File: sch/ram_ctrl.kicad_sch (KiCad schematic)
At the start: 12 parts

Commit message: RAM ctrl updates
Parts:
- gave numbers to parts that had none: 1
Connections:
- net z4: now reaches D48.1 (~{R}), D49.10 (O5)
- net at D48.6 (~{Q}): now also D18.2
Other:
- note added: "FIXME: z5 or z6 ?!"
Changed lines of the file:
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@@
+    (stroke (width 0) (type default) (color 0 0 0 0))
+  )
+  (wire (pts (xy 225.425 90.17) (xy 227.965 90.17))
     (stroke (width 0) (type default) (color 0 0 0 0))
   )
@@
     (stroke (width 0) (type default) (color 0 0 0 0))
   )
+  (text "FIXME: z5 or z6 ?!" (at 53.975 147.955 0)
+    (effects (font (size 1.27 1.27)) (justify left bottom))
+  )
   (label "VIDEO-CPU" (at 51.435 137.16 0)
     (effects (font (size 1.27 1.27)) (justify left bottom))
@@
   )
   (label "t2" (at 150.495 62.23 0)
+    (effects (font (size 1.27 1.27)) (justify left bottom))
+  )
+  (label "z4" (at 199.39 69.85 0)
     (effects (font (size 1.27 1.27)) (justify left bottom))
   )
@@
     (pin "1")
   )
-  (symbol (lib_id "74xx:74LS08") (at 162.56 138.43 0) (unit 3) (convert 2)
+  (symbol (lib_id "74xx:74LS08") (at 162.56 138.43 0) (unit 3)
     (in_bom yes) (on_board yes)
     (property "Reference" "D47" (id 0) (at 161.925 143.51 0))
@@
   (symbol (lib_id "74xx:74LS74") (at 247.015 66.04 0) (unit 2)
     (in_bom yes) (on_board yes) (fields_autoplaced)
-    (property "Reference" "D?" (id 0) (at 249.0344 55.88 0)
-      (effects (font (size 1.27 1.27)) (justify left))
-    )
+    (property "Reference" "D48" (id 0) (at 249.0344 55.88 0)
+      (effects (font (size 1.27 1.27)) (justify left))
+    )

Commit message: RAM controller - rework
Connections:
- net VIDEO_CPU: no longer D42.13 (~{R}), D42.4 (~{S})
- new net VIDEO-CPU: D42.13 (~{R}), D42.4 (~{S})
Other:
- moved on the sheet: D18A, D18B, D33D, D33F, D42A, D42B, D46A, D46B, D47A, D47C, D48A, D48B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

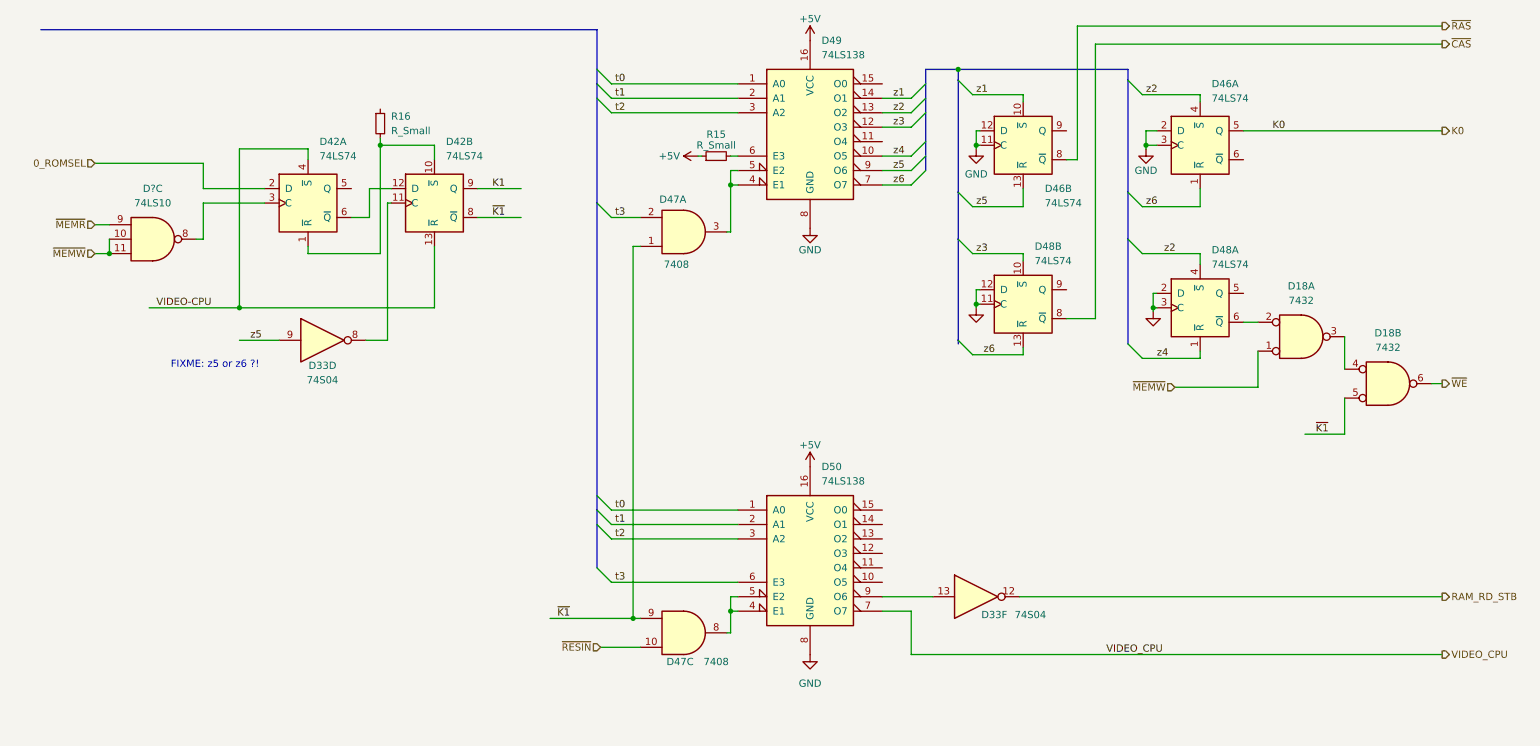
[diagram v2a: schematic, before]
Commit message: RAM ctrl schematic cleanup completed
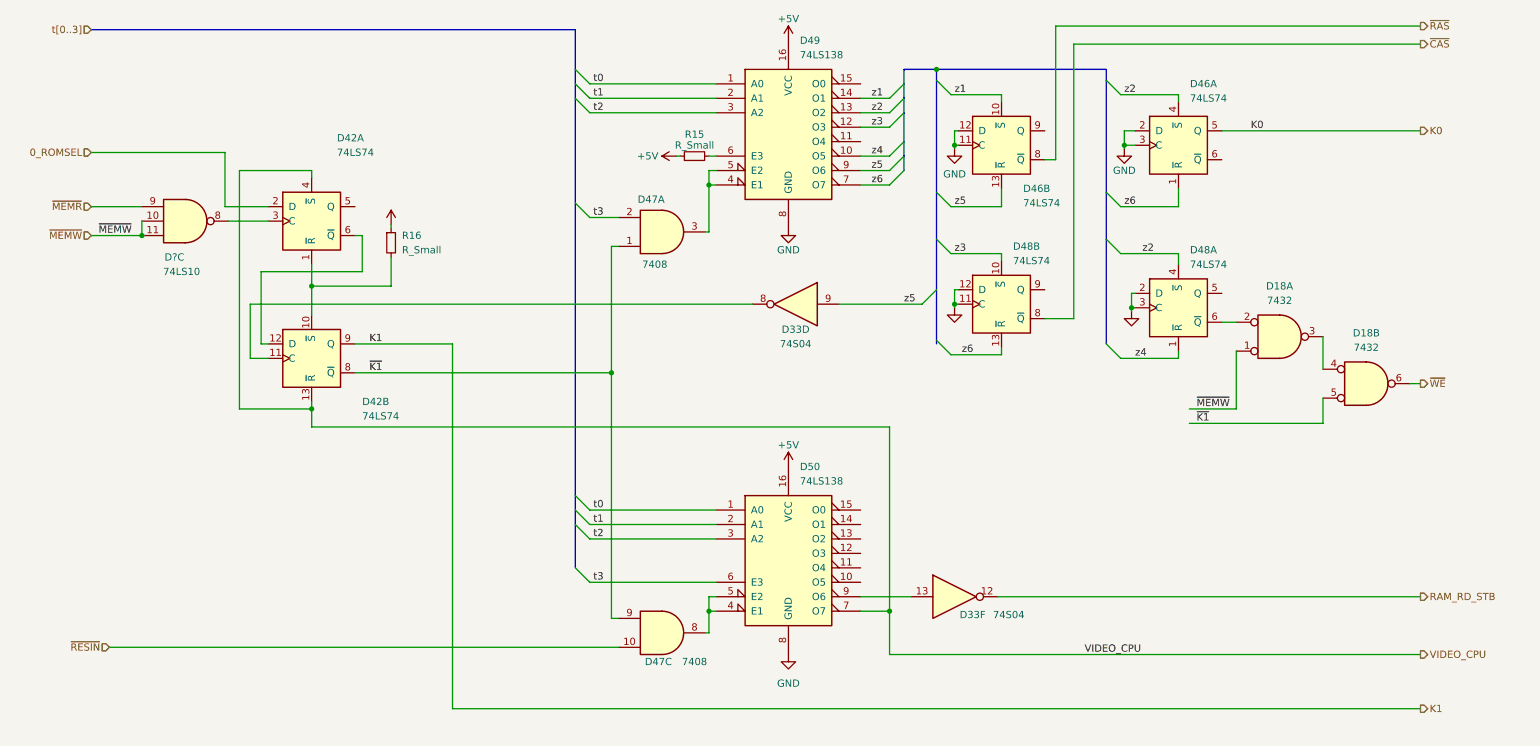
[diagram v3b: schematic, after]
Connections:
- net VIDEO-CPU is gone; now on net VIDEO_CPU: D42.13 (~{R}), D42.4 (~{S})
- net +5V: now also R16.1
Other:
- note removed: "FIXME: z5 or z6 ?!"
- moved on the sheet: D18A, D18B, D33D, D33F, D42A, D42B, D46A, D46B, D47A, D47C, D48A, D48B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

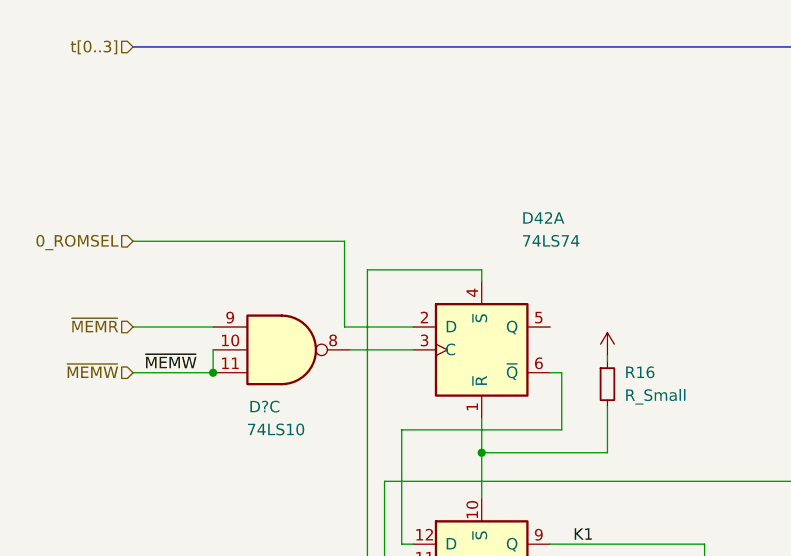
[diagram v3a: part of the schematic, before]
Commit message: Sch: timing counters block completed
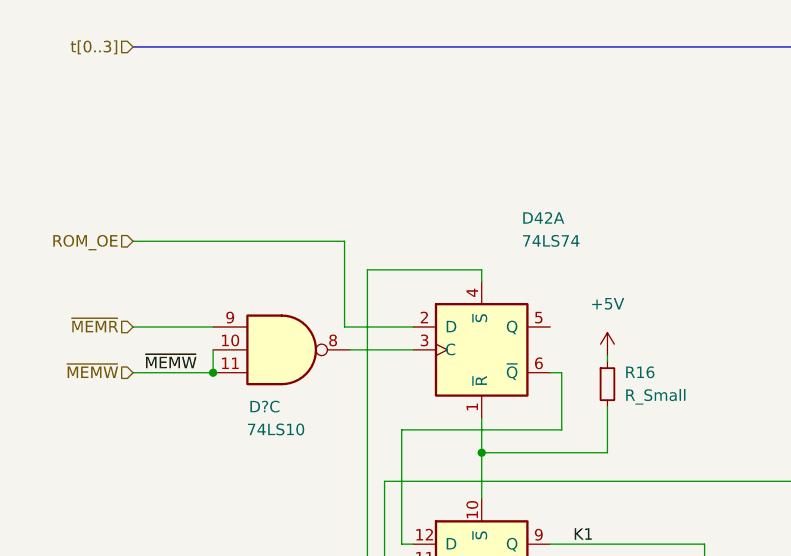
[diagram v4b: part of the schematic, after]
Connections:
- net 0_ROMSEL renamed ROM_OE
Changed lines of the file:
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@@
     (effects (font (size 1.27 1.27)) (justify left))
   )
-  (hierarchical_label "0_ROMSEL" (shape input) (at 31.115 48.895 180)
+  (hierarchical_label "ROM_OE" (shape input) (at 31.115 48.895 180)
     (effects (font (size 1.27 1.27)) (justify right))
   )
@@
       (effects (font (size 1.27 1.27)) hide)
     )
-    (property "Value" "" (id 1) (at 83.82 55.88 0))
+    (property "Value" "+5V" (id 1) (at 83.82 55.88 0))
     (property "Footprint" "" (id 2) (at 83.82 61.595 0)
       (effects (font (size 1.27 1.27)) hide)

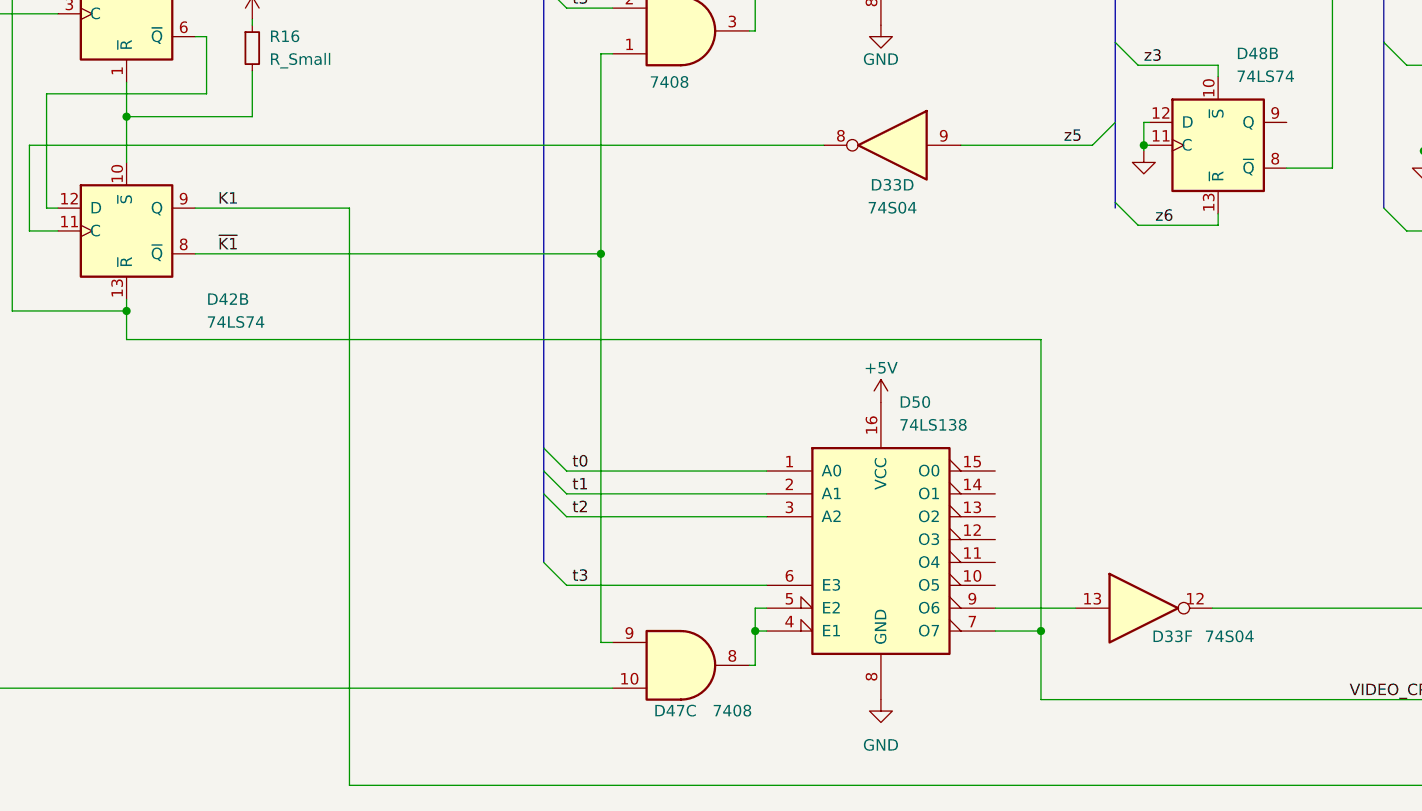
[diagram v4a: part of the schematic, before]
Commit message: Sch: video block rework
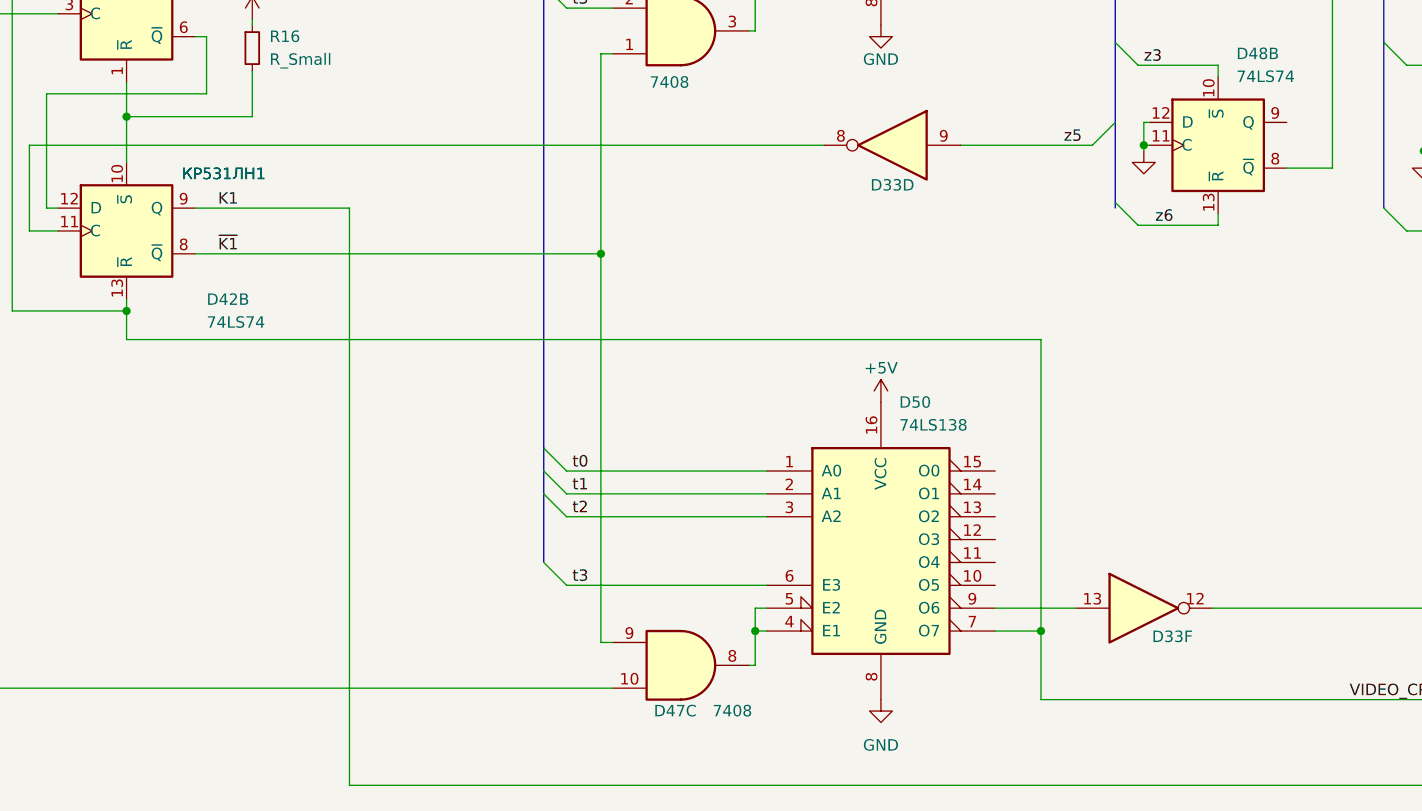
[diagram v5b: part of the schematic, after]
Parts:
- D33: value 74S04 -> (none); CCCP (none) -> КР531ЛН1
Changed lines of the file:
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@@
     (in_bom yes) (on_board yes)
     (property "Reference" "D33" (id 0) (at 154.94 80.01 0))
-    (property "Value" "74S04" (id 1) (at 154.94 82.55 0))
+    (property "Value" "" (id 1) (at 154.94 82.55 0))
     (property "Footprint" "" (id 2) (at 154.94 75.565 0)
       (effects (font (size 1.27 1.27)) hide)
@@
       (effects (font (size 1.27 1.27)) hide)
     )
+    (property "CCCP" "КР531ЛН1" (id 4) (at 80.645 78.74 0))
     (pin "1")
     (pin "2")
@@
     (in_bom yes) (on_board yes)
     (property "Reference" "D33" (id 0) (at 186.055 130.175 0))
-    (property "Value" "74S04" (id 1) (at 192.405 130.175 0))
+    (property "Value" "" (id 1) (at 192.405 130.175 0))
     (property "Footprint" "" (id 2) (at 182.88 127 0)
       (effects (font (size 1.27 1.27)) hide)
@@
       (effects (font (size 1.27 1.27)) hide)
     )
+    (property "CCCP" "КР531ЛН1" (id 4) (at 80.645 78.74 0))
     (pin "1")
     (pin "2")

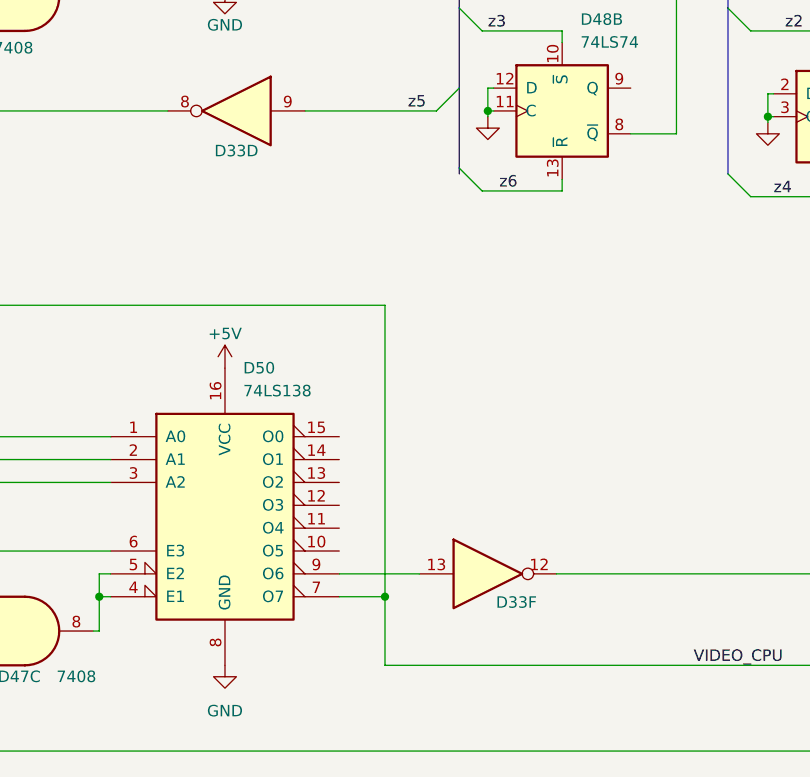
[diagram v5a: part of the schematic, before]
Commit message: Sch: video block cleanup in progress
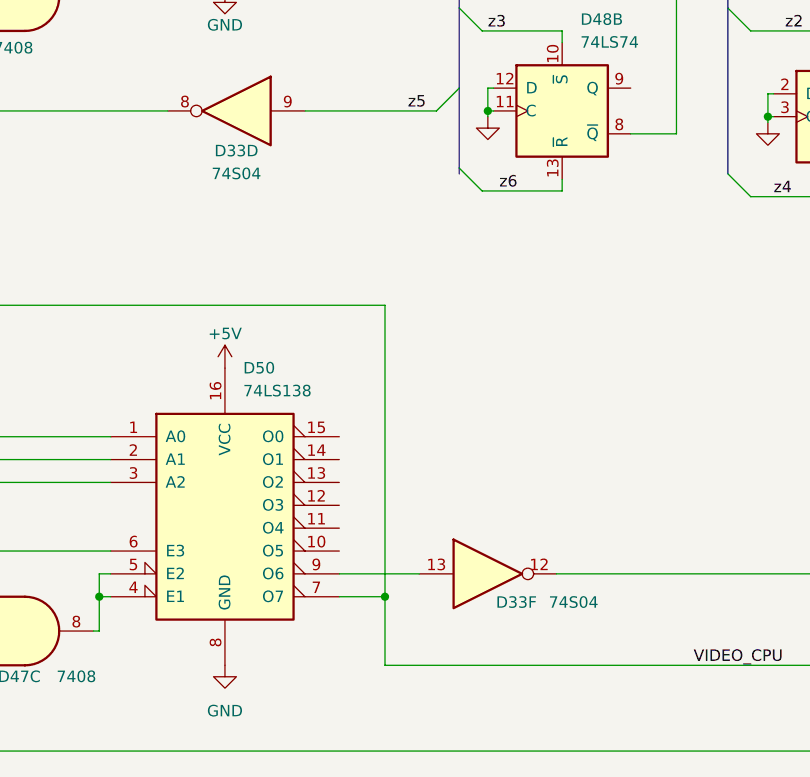
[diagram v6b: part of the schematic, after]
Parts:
- D33: value (none) -> 74S04
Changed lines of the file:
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@@
     (in_bom yes) (on_board yes)
     (property "Reference" "D33" (id 0) (at 154.94 80.01 0))
-    (property "Value" "" (id 1) (at 154.94 82.55 0))
+    (property "Value" "74S04" (id 1) (at 154.94 82.55 0))
     (property "Footprint" "" (id 2) (at 154.94 75.565 0)
       (effects (font (size 1.27 1.27)) hide)
@@
     (in_bom yes) (on_board yes)
     (property "Reference" "D33" (id 0) (at 186.055 130.175 0))
-    (property "Value" "" (id 1) (at 192.405 130.175 0))
+    (property "Value" "74S04" (id 1) (at 192.405 130.175 0))
     (property "Footprint" "" (id 2) (at 182.88 127 0)
       (effects (font (size 1.27 1.27)) hide)
